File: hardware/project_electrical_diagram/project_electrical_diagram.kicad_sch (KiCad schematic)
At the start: 4 parts, among them U2 ESP32-WROOM-32_devkit

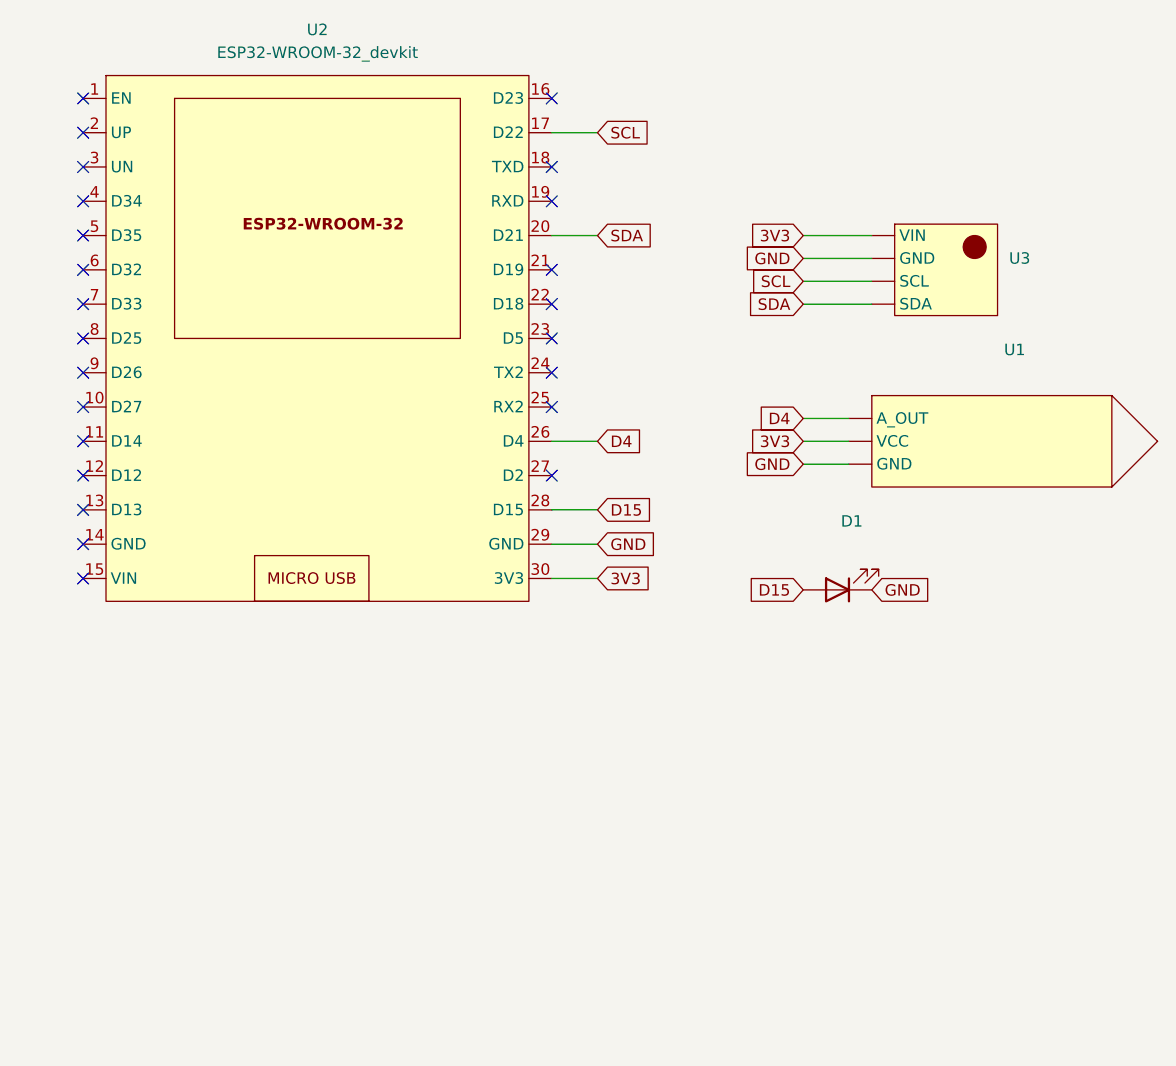
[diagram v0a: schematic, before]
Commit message: [hardware] updated diagram
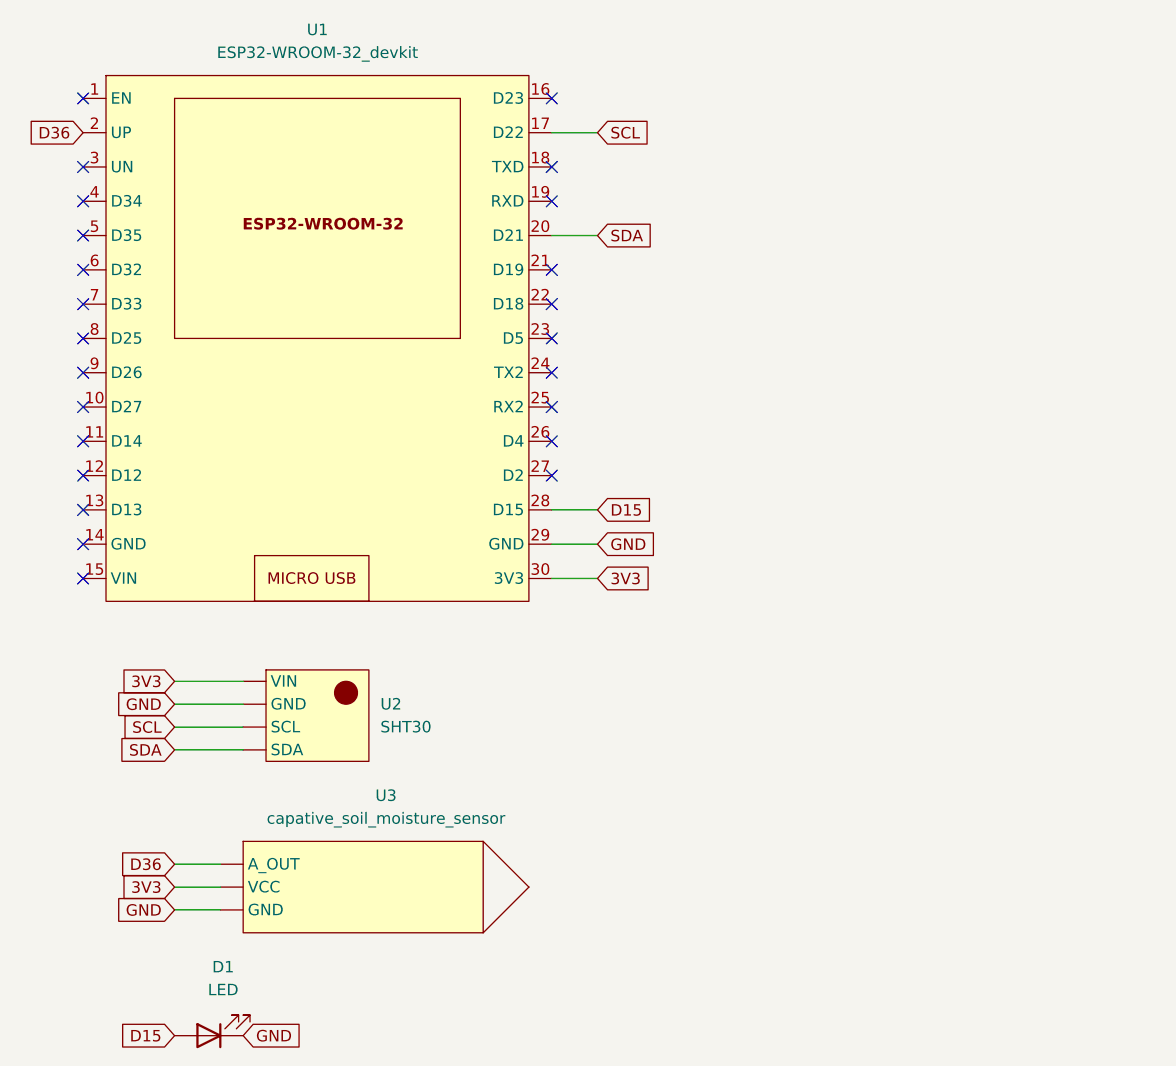
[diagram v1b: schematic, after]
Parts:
- removed U1: (no value), symbol my_symbol_lib:capative_soil_moisture_sensor
- removed U3: (no value), symbol my_symbol_lib:SHT30
- added U2: SHT30, symbol my_symbol_lib:SHT30
- added U3: capative_soil_moisture_sensor, symbol my_symbol_lib:capative_soil_moisture_sensor
- D1: value (none) -> LED
- renumbered U2 to U1
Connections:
- net 3V3: now also U2. (VIN), U3. (VCC)
- net GND: now also U2. (VIN), U3. (VCC)
- net SCL: now also U2. (VIN)
- net SDA: now also U2. (VIN)
- net D36: now reaches U1.2 (UP)
- net D36: now also U3. (VCC)
- net D4: no longer names the net of U1.26 (D4)
